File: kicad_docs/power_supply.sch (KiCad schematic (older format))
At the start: 10 parts, among them J1 power_in, U6 LM1117-3.3

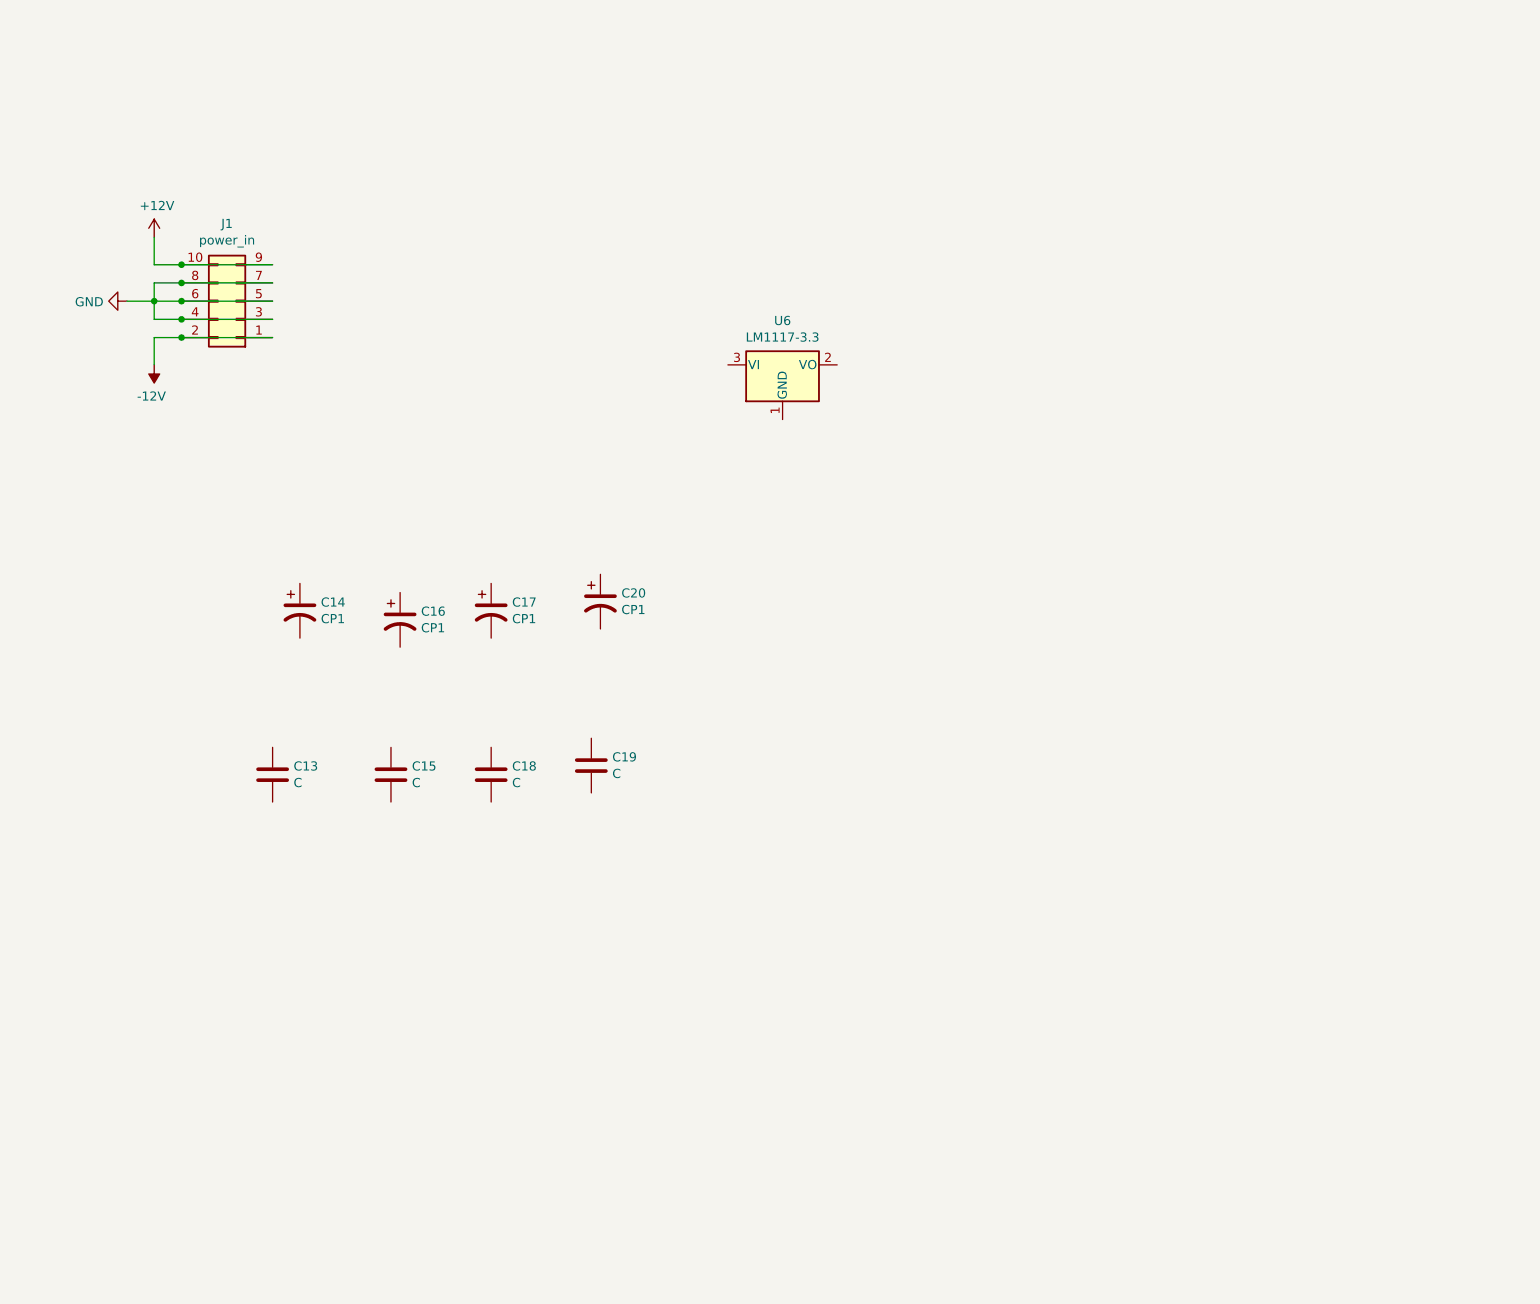
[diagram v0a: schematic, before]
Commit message: add EEPROM, big pcb re-design
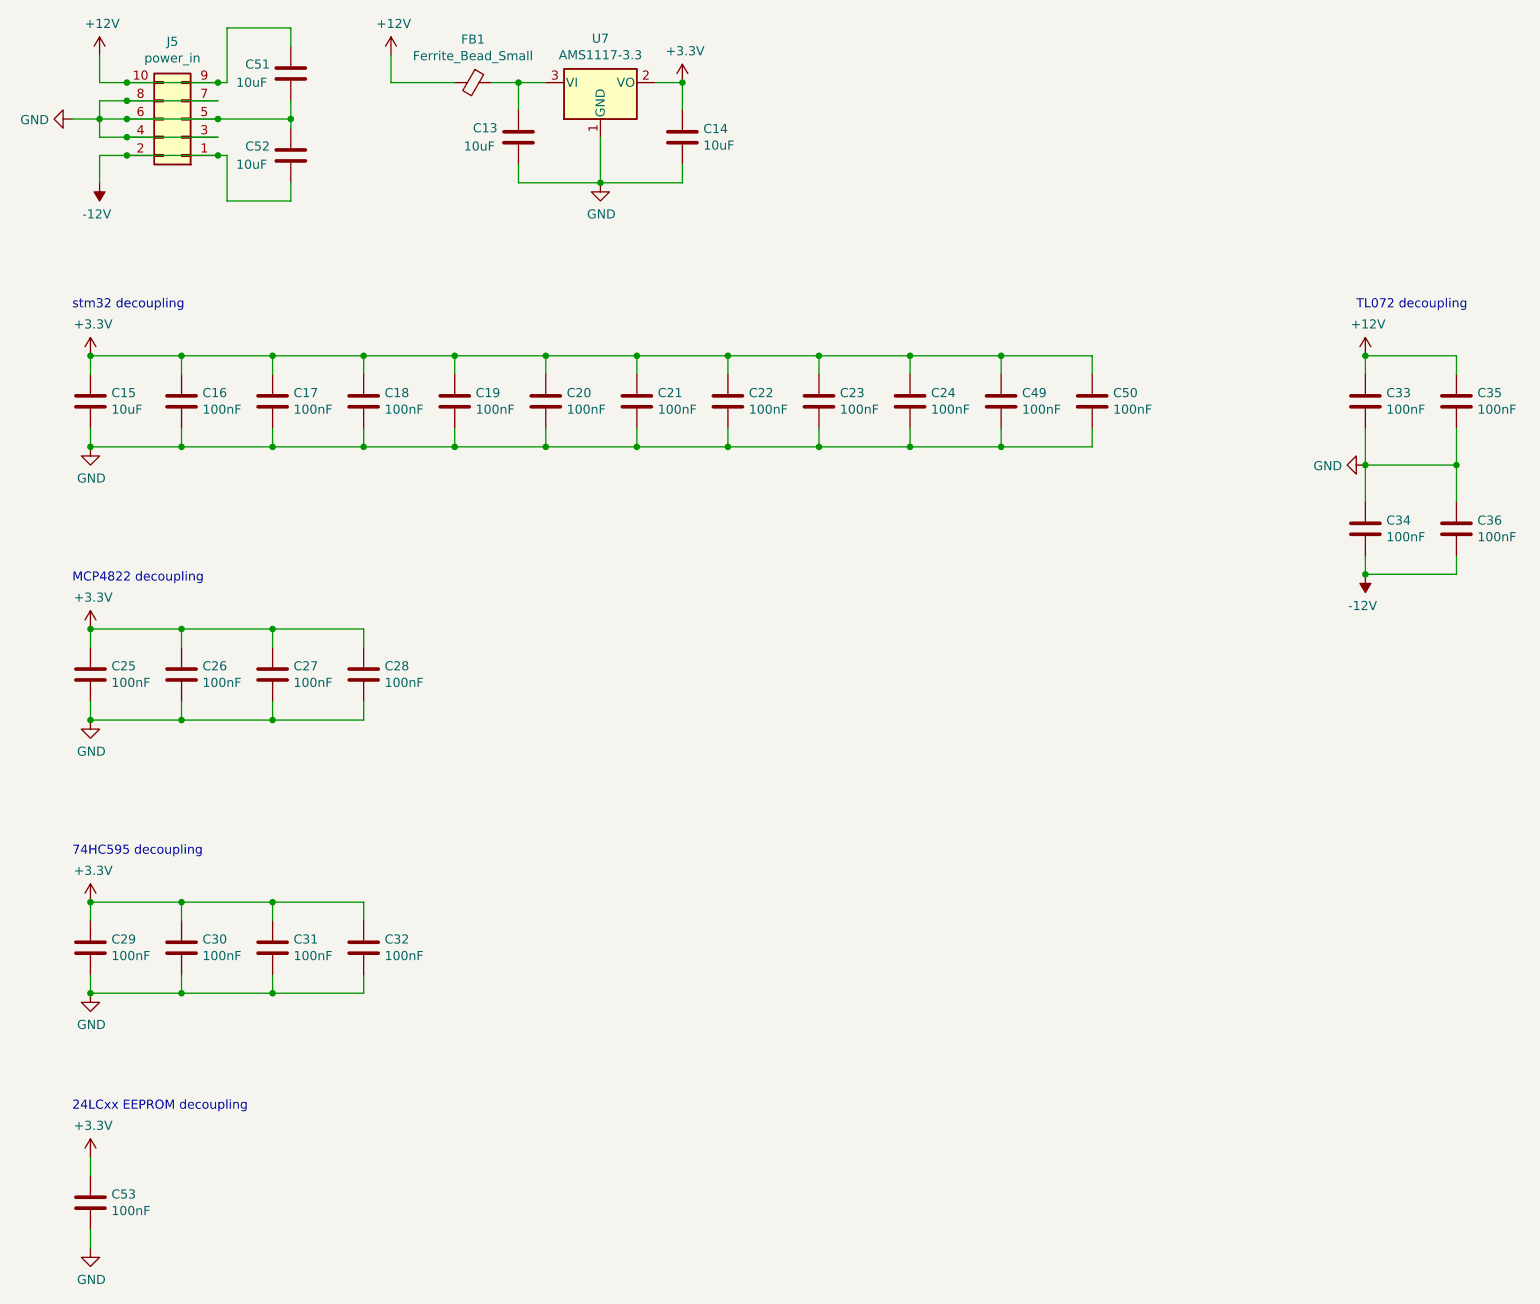
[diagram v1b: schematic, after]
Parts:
- removed C14, C16, C17, C20: CP1, Capacitor_SMD:CP_Elec_5x5.4, symbol Device:CP1
- removed U6: LM1117-3.3, Package_TO_SOT_SMD:SOT-223-3_TabPin2, symbol Regulator_Linear:LM1117-3.3
- added C14: 10uF, Capacitor_SMD:C_0805_2012Metric, symbol Device:C
- added C16, C17, C20, C21, C22, C23, C24, C25, C26, C27, C28, C29, C30, C31, C32, C49, C50, C53: 100nF, Capacitor_SMD:C_0402_1005Metric, symbol Device:C
- added C33, C34, C35, C36: 100nF, Capacitor_SMD:C_0603_1608Metric, symbol Device:C
- added C51, C52: 10uF, Capacitor_SMD:C_1206_3216Metric, symbol Device:C
- added FB1: Ferrite_Bead_Small, Inductor_SMD:L_0805_2012Metric, symbol Device:Ferrite_Bead_Small
- added U7: AMS1117-3.3, Package_TO_SOT_SMD:SOT-223-3_TabPin2, symbol Regulator_Linear:AMS1117-3.3
- C13: value C -> 10uF; footprint Capacitor_SMD:C_0805_2012Metric_Pad1.15x1.40mm_HandSolder -> Capacitor_SMD:C_1206_3216Metric
- C15: value C -> 10uF; footprint Capacitor_SMD:C_0805_2012Metric_Pad1.15x1.40mm_HandSolder -> Capacitor_SMD:C_0805_2012Metric
- C18, C19: value C -> 100nF; footprint Capacitor_SMD:C_0805_2012Metric_Pad1.15x1.40mm_HandSolder -> Capacitor_SMD:C_0402_1005Metric
- renumbered J1 to J5
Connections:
- net +12V: now also C33.1, C35.1, C51.1, FB1.2
- net -12V: now also C34.2, C36.2, C52.2
- net GND: now also C13.2, C15.2, C18.2, C19.2, C14.2, C16.2, C17.2, C20.2, C21.2, C22.2, C23.2, C24.2, C25.2, C26.2, C27.2, C28.2, C29.2, C30.2, C31.2, C32.2, C33.2, C34.1, C35.2, C36.1, C49.2, C50.2, C51.2, C52.1, C53.2, U7.1 (GND)
- net at C13.1: now also FB1.1, U7.3 (VI)
- net +3V3: now reaches C15.1
- net +3V3: now also C18.1, C19.1, C14.1, C16.1, C17.1, C20.1, C21.1, C22.1, C23.1, C24.1, C25.1, C26.1, C27.1, C28.1, C29.1, C30.1, C31.1, C32.1, C49.1, C50.1, C53.1, U7.2 (VO)
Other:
- note added: "24LCxx EEPROM decoupling"
- note added: "74HC595 decoupling"
- note added: "MCP4822 decoupling"
- note added: "TL072 decoupling"
- note added: "stm32 decoupling"
- moved on the sheet: J5
